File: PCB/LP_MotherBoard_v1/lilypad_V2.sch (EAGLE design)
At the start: 27 parts, among them U2 INA169, X4 BQ24074

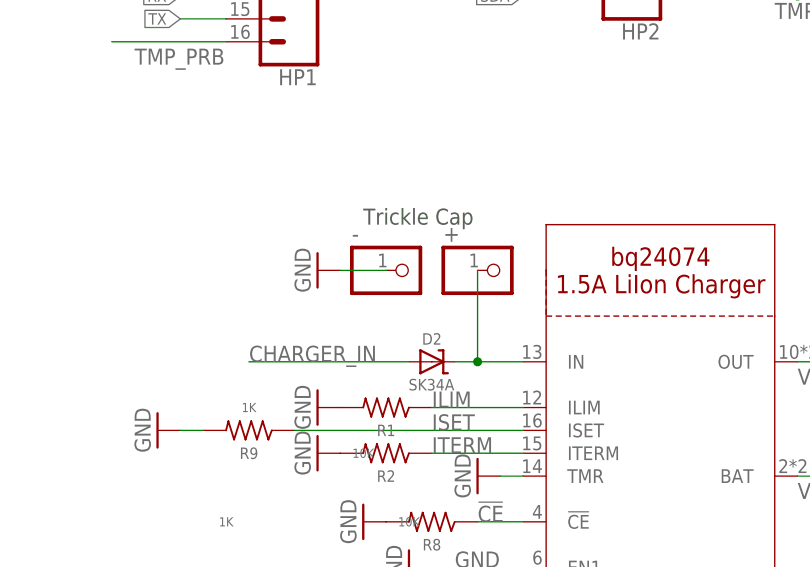
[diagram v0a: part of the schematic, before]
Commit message: Fixed some sch errors
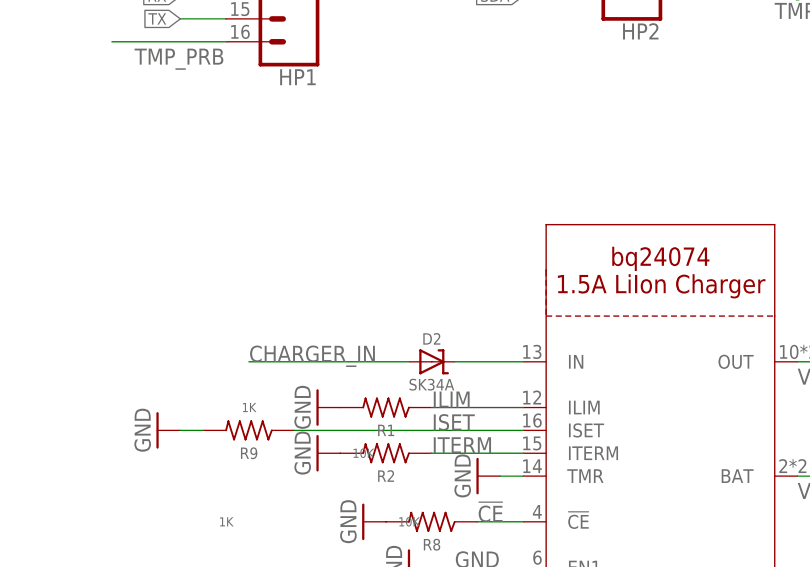
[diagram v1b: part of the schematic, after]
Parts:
- removed +, -: (no value), microbuilder:HEADER-1X1
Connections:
- net GND: no longer -.1
- net N$2: no longer +.1
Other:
- note removed: "Trickle Cap"
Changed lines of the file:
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@@
 </groups>
 <parts>
-<part name="GND16" library="supply1" deviceset="GND" device=""/>
-<part name="-" library="microbuilder" deviceset="HEADER-1X1" device=""/>
-<part name="+" library="microbuilder" deviceset="HEADER-1X1" device=""/>
 <part name="BATT" library="adafruit" deviceset="JST_2PIN" device="-SMT-RA" value="JST 2PH"/>
 <part name="GND6" library="supply1" library_urn="urn:adsk.eagle:library:371" deviceset="GND" device=""/>
@@
 <plain>
 <text x="187.96" y="121.92" size="1.778" layer="97" grouprefs="SENSOR_CONNECTORS">DS18B20</text>
-<text x="142.24" y="81.28" size="1.778" layer="97" grouprefs="SOLAR_CHARGER">Trickle Cap</text>
 <text x="198.12" y="33.02" size="1.778" layer="97" grouprefs="SOLAR_CHARGER">Batt tmp probe</text>
 <text x="210.82" y="71.12" size="1.778" layer="97" grouprefs="SOLAR_CHARGER">Battery input</text>
@@
 </plain>
 <instances>
-<instance part="GND16" gate="1" x="137.16" y="76.2" smashed="yes" rot="R270" grouprefs="SOLAR_CHARGER">
-<attribute name="VALUE" x="134.62" y="78.74" size="1.778" layer="96" rot="R270"/>
-</instance>
-<instance part="-" gate="G$1" x="147.32" y="76.2" smashed="yes" grouprefs="SOLAR_CHARGER">
-<attribute name="NAME" x="140.97" y="79.375" size="1.778" layer="95"/>
-<attribute name="VALUE" x="140.97" y="71.12" size="1.778" layer="96"/>
-</instance>
-<instance part="+" gate="G$1" x="157.48" y="76.2" smashed="yes" grouprefs="SOLAR_CHARGER">
-<attribute name="NAME" x="151.13" y="79.375" size="1.778" layer="95"/>
-<attribute name="VALUE" x="151.13" y="71.12" size="1.778" layer="96"/>
-</instance>
 <instance part="BATT" gate="G$1" x="231.14" y="60.96" smashed="yes" rot="MR180" grouprefs="SOLAR_CHARGER">
 <attribute name="NAME" x="224.79" y="55.245" size="1.778" layer="95" rot="MR180"/>
@@
 <nets>
 <net name="GND" class="0">
-<segment>
-<pinref part="GND16" gate="1" pin="GND"/>
-<pinref part="-" gate="G$1" pin="1"/>
-<wire x1="144.78" y1="76.2" x2="139.7" y2="76.2" width="0.1524" layer="91" grouprefs="SOLAR_CHARGER"/>
-</segment>
 <segment>
 <wire x1="220.98" y1="58.42" x2="228.6" y2="58.42" width="0.1524" layer="91" grouprefs="SOLAR_CHARGER"/>
@@
 <pinref part="X4" gate="G$1" pin="IN"/>
 <pinref part="D2" gate="G$1" pin="C"/>
-<wire x1="160.02" y1="66.04" x2="154.94" y2="66.04" width="0.1524" layer="91" grouprefs="SOLAR_CHARGER"/>
-<pinref part="+" gate="G$1" pin="1"/>
-<wire x1="154.94" y1="66.04" x2="152.4" y2="66.04" width="0.1524" layer="91" grouprefs="SOLAR_CHARGER"/>
-<wire x1="154.94" y1="76.2" x2="154.94" y2="66.04" width="0.1524" layer="91" grouprefs="SOLAR_CHARGER"/>
-<junction x="154.94" y="66.04" grouprefs="SOLAR_CHARGER"/>
-</segment>
-</net>
+<wire x1="160.02" y1="66.04" x2="152.4" y2="66.04" width="0.1524" layer="91" grouprefs="SOLAR_CHARGER"/>
+</segment>
+</net>

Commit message: Lilypad PCB Post Review and README
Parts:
- added J2: (no value), SparkFun-Connectors:M04PTH
- added JP1: (no value), adafruit:PINHD-1X3
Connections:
- new net VIN: HP2.1, JP1.2
- net GND: now also J2.2
- net SCL: now also J2.3
- net SDA: now also J2.4
- net VBAT: now also JP1.3; no longer HP2.1
- net VCC: now also J2.1
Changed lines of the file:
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@@
 <part name="RED" library="adafruit" library_urn="urn:adsk.eagle:library:420" deviceset="LED" device="SMT1206" package3d_urn="urn:adsk.eagle:package:6240349/1"/>
 <part name="GREEN" library="adafruit" library_urn="urn:adsk.eagle:library:420" deviceset="LED" device="SMT1206" package3d_urn="urn:adsk.eagle:package:6240349/1"/>
+<part name="J2" library="SparkFun-Connectors" deviceset="M04" device="PTH"/>
+<part name="JP1" library="adafruit" library_urn="urn:adsk.eagle:library:420" deviceset="PINHD-1X3" device="" package3d_urn="urn:adsk.eagle:package:6240710/1"/>
 </parts>
 <sheets>
@@
 <text x="83.82" y="53.34" size="1.778" layer="91" grouprefs="INA169_MULTIMETER">Solar Hookup</text>
 <text x="205.74" y="139.7" size="1.778" layer="97" grouprefs="SENSOR_CONNECTORS">I2C</text>
+<text x="228.6" y="139.7" size="1.778" layer="97" grouprefs="SENSOR_CONNECTORS">I2C</text>
 </plain>
 <instances>
@@
 <attribute name="NAME" x="129.032" y="39.116" size="1.778" layer="95" rot="R180"/>
 <attribute name="VALUE" x="129.032" y="41.275" size="1.778" layer="96" rot="R180"/>
+</instance>
+<instance part="J2" gate="G$1" x="215.9" y="132.08" smashed="yes" grouprefs="SENSOR_CONNECTORS">
+<attribute name="VALUE" x="210.82" y="124.46" size="1.778" layer="96"/>
+<attribute name="NAME" x="210.82" y="140.462" size="1.778" layer="95"/>
+</instance>
+<instance part="JP1" gate="A" x="200.66" y="73.66" smashed="yes">
+<attribute name="NAME" x="194.31" y="79.375" size="1.778" layer="95"/>
+<attribute name="VALUE" x="194.31" y="66.04" size="1.778" layer="96"/>
 </instance>
 </instances>
@@
 <pinref part="GND1" gate="1" pin="GND"/>
 </segment>
+<segment>
+<pinref part="J2" gate="G$1" pin="2"/>
+<wire x1="220.98" y1="132.08" x2="228.6" y2="132.08" width="0.1524" layer="91" grouprefs="SENSOR_CONNECTORS"/>
+<label x="223.52" y="132.08" size="1.778" layer="95" grouprefs="SENSOR_CONNECTORS"/>
+</segment>
 </net>
 <net name="THERM" class="0">
@@
 <label x="200.66" y="134.62" size="1.778" layer="95" grouprefs="SENSOR_CONNECTORS"/>
 </segment>
+<segment>
+<pinref part="J2" gate="G$1" pin="3"/>
+<wire x1="220.98" y1="134.62" x2="228.6" y2="134.62" width="0.1524" layer="91" grouprefs="SENSOR_CONNECTORS"/>
+<label x="223.52" y="134.62" size="1.778" layer="95" grouprefs="SENSOR_CONNECTORS"/>
+</segment>
 </net>
 <net name="SDA" class="0">
@@
 <wire x1="198.12" y1="137.16" x2="205.74" y2="137.16" width="0.1524" layer="91" grouprefs="SENSOR_CONNECTORS"/>
 <label x="200.66" y="137.16" size="1.778" layer="95" grouprefs="SENSOR_CONNECTORS"/>
+</segment>
+<segment>
+<pinref part="J2" gate="G$1" pin="4"/>
+<wire x1="220.98" y1="137.16" x2="228.6" y2="137.16" width="0.1524" layer="91" grouprefs="SENSOR_CONNECTORS"/>
+<label x="223.52" y="137.16" size="1.778" layer="95" grouprefs="SENSOR_CONNECTORS"/>
 </segment>
 </net>
@@
 <junction x="15.24" y="60.96" grouprefs="INA169_MULTIMETER"/>
 </segment>
+<segment>
+<pinref part="J2" gate="G$1" pin="1"/>
+<wire x1="220.98" y1="129.54" x2="228.6" y2="129.54" width="0.1524" layer="91" grouprefs="SENSOR_CONNECTORS"/>
+<label x="223.52" y="129.54" size="1.778" layer="95" grouprefs="SENSOR_CONNECTORS"/>
+</segment>
 </net>
 <net name="EN" class="0">
@@
 <net name="VBAT" class="0">
 <segment>
-<pinref part="HP2" gate="G$1" pin="1"/>
-<wire x1="165.1" y1="134.62" x2="154.94" y2="134.62" width="0.1524" layer="91" grouprefs="HYPNOS1"/>
-<label x="154.94" y="134.62" size="1.27" layer="95" rot="R180" xref="yes" grouprefs="HYPNOS1"/>
-</segment>
-<segment>
 <pinref part="X4" gate="G$1" pin="OUT"/>
-<wire x1="190.5" y1="66.04" x2="195.58" y2="66.04" width="0.1524" layer="91" grouprefs="SOLAR_CHARGER"/>
+<wire x1="190.5" y1="66.04" x2="198.12" y2="66.04" width="0.1524" layer="91" grouprefs="SOLAR_CHARGER"/>
 <label x="190.5" y="63.5" size="1.778" layer="95" grouprefs="SOLAR_CHARGER"/>
+<pinref part="JP1" gate="A" pin="3"/>
+<wire x1="198.12" y1="66.04" x2="198.12" y2="71.12" width="0.1524" layer="91"/>
 </segment>
 <segment>
@@
 </segment>
 </net>
+<net name="VIN" class="0">
+<segment>
+<pinref part="JP1" gate="A" pin="2"/>
+<wire x1="198.12" y1="73.66" x2="193.04" y2="73.66" width="0.1524" layer="91"/>
+<label x="190.5" y="73.66" size="1.778" layer="95"/>
+</segment>
+<segment>
+<pinref part="HP2" gate="G$1" pin="1"/>
+<wire x1="165.1" y1="134.62" x2="154.94" y2="134.62" width="0.1524" layer="91" grouprefs="HYPNOS1"/>
+<label x="154.94" y="134.62" size="1.27" layer="95" rot="R180" xref="yes" grouprefs="HYPNOS1"/>
+</segment>
+</net>
